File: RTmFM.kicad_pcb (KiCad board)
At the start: 2 copper layers, 122 x 157 mm, 58 parts, among them J1 Conn_02x04_Odd_Even, J2 Conn_01x04, J3 Conn_02x17_Odd_Even, J4 Conn_02x10_Odd_Even, J5 Micro_SD_Card, J6 Conn_01x02, J7 Conn_01x02, U1 SN75176AP, U10 74LS06, U2 SN75176AP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

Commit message: Almost finished HW design
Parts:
- U10, U9: footprint Package_DIP:DIP-14_W10.16mm -> Package_DIP:DIP-14_W7.62mm
- moved J4 143.4 mm to (173.4, 40.2), turned to -90 degrees
- moved J2 130.1 mm to (32.7, 35.5), turned to 0 degrees
- moved U2 126.7 mm to (172.8, 57.2), turned to -90 degrees
- moved C7 125.8 mm to (176.6, 63.4), turned to 90 degrees
- moved R29 121.9 mm to (85.4, 71.1), turned to 180 degrees
- moved R2 117.6 mm to (30.0, 71.2), turned to 0 degrees
- moved C8 113.0 mm to (102.0, 76.2), turned to 180 degrees
- moved R28 111.5 mm to (85.4, 79.1), turned to 180 degrees
- moved J3 111.4 mm to (134.4, 40.2), turned to -90 degrees
- moved C2 111.1 mm to (176.6, 88.8), turned to 90 degrees
- moved U1 110.5 mm to (157.5, 57.2), turned to -90 degrees
- moved U7 109.0 mm to (172.8, 82.5), turned to -90 degrees
- moved C6 108.5 mm to (161.3, 63.5), turned to 90 degrees
- moved R3 106.8 mm to (30.0, 79.2), turned to 0 degrees
- moved R10 104.7 mm to (165.1, 74.9), turned to 0 degrees
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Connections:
- U10 pad 3: /TRACK0 -> /WRITE_FAULT
- U10 pad 4: /ocTRACK0 -> /ocWRITE_FAULT
- U10 pad 5: /WRITE_FAULT -> /INDEX
- U10 pad 6: /ocWRITE_FAULT -> /ocINDEX
- U10 pad 8: /ocINDEX -> /ocTRACK0
- U10 pad 9: /INDEX -> /TRACK0
- U8 pad 39: unconnected-(U8-VSYS-Pad39) -> VCC
- U9 pad 1: /HEAD0 -> /HEAD1
- U9 pad 2: /HSEL0 -> /HSEL1
- U9 pad 3: /HEAD1 -> /HEAD0
- U9 pad 4: /HSEL1 -> /HSEL0
- U9 pad 5: /HEAD2 -> (no net)
- U9 pad 6: /HSEL2 -> (no net)
- U9 pad 8: /RDENA -> /HSEL2
- U9 pad 9: /WRGATE -> /HEAD2
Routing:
- net VCC: track 271.4 -> 620.0 mm, vias 0 -> 4
- net GND: track 0.00 -> 144.0 mm, vias 0 -> 1
- net /DSEL: track 0.00 -> 143.9 mm, vias 0 -> 2
- net /DOUT: track 0.00 -> 110.5 mm, vias 0 -> 1
- net /WDATA: track 0.00 -> 95.3 mm, vias 0 -> 1
- net +12V: track 133.8 -> 217.6 mm
- net /STEP: track 30.4 -> 105.1 mm, vias 0 -> 3
- net /HSEL0: track 0.00 -> 66.9 mm, vias 0 -> 1
- net Net-(J6-Pin_2): track 0.00 -> 63.5 mm, vias 0 -> 1
- net /HSEL2: track 0.00 -> 61.6 mm, vias 0 -> 1
- net /SD_DAT1: track 0.00 -> 60.2 mm
- net /TRACK0: track 16.8 -> 76.8 mm
- net /DIRECTION: track 34.5 -> 93.9 mm, vias 1 -> 3
- net /HSEL1: track 0.00 -> 59.2 mm, vias 0 -> 1
- net /DRV_LED: track 0.00 -> 57.5 mm, vias 0 -> 1
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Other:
- board size 122 x 157 mm -> 157 x 122 mm
- board text added: "+"
- board text added: "0"
- board text added: "1"
- board text added: "12V DUMMY LOAD"
- board text added: "2"
- board text added: "3"
- board text added: "5V DUMMY LOAD"
- board text added: "ACT LED"
- board text added: "DRIVE SELECT"
- board text added: "Designed By Majenko"
- board text added: "M"
- board text added: "RTmFM MFM Emulator Version 1.0"
- board text added: "T"
- board text added: "TERM EN"
- board text added: "majenko.co.uk"

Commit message: End of version 1 design
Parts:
- added H1: MountingHole, MountingHole:MountingHole_3.2mm_M3_DIN965_Pad_TopBottom, F.Cu at (31.0, 45.0)
- added H2: MountingHole, MountingHole:MountingHole_3.2mm_M3_DIN965_Pad_TopBottom, F.Cu at (179.0, 45.0)
- added H3: MountingHole, MountingHole:MountingHole_3.2mm_M3_DIN965_Pad_TopBottom, F.Cu at (31.0, 148.0)
- added H4: MountingHole, MountingHole:MountingHole_3.2mm_M3_DIN965_Pad_TopBottom, F.Cu at (179.0, 148.0)
- added J8: Conn_01x10, Connector_PinHeader_2.54mm:PinHeader_1x10_P2.54mm_Vertical, F.Cu at (165.1, 96.5)
- added R30: 100R, Resistor_THT:R_Axial_DIN0204_L3.6mm_D1.6mm_P7.62mm_Horizontal, F.Cu at (150.0, 106.7)
- added R31: 100R, Resistor_THT:R_Axial_DIN0204_L3.6mm_D1.6mm_P7.62mm_Horizontal, F.Cu at (150.0, 109.2)
- added R32: 100R, Resistor_THT:R_Axial_DIN0204_L3.6mm_D1.6mm_P7.62mm_Horizontal, F.Cu at (150.0, 111.8)
- added R33: 100R, Resistor_THT:R_Axial_DIN0204_L3.6mm_D1.6mm_P7.62mm_Horizontal, F.Cu at (150.0, 114.3)
- added R34: 100R, Resistor_THT:R_Axial_DIN0204_L3.6mm_D1.6mm_P7.62mm_Horizontal, F.Cu at (150.0, 116.8)
- moved R18 6.16 mm to (30.0, 129.0)
- moved R19 6.16 mm to (30.0, 137.0)
- moved R20 6.16 mm to (85.4, 137.0)
- moved R21 6.16 mm to (85.4, 129.0)
- moved R14 6.16 mm to (30.0, 97.0)
- moved R15 6.16 mm to (30.0, 105.0)
- moved R16 6.16 mm to (30.0, 113.0)
- moved R17 6.16 mm to (30.0, 121.0)
- moved R2 6.16 mm to (30.0, 65.0)
- moved R22 6.16 mm to (85.4, 121.0)
- moved R23 6.16 mm to (85.4, 113.0)
- moved R24 6.16 mm to (85.4, 105.0)
- moved R25 6.16 mm to (85.4, 97.0)
- moved R26 6.16 mm to (85.4, 89.0)
- moved R27 6.16 mm to (85.4, 81.0)
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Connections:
- U8 pad 10: unconnected-(U8-GPIO7-Pad10) -> /pSTEP
- U8 pad 11: /DSEL -> /pDIRECTION
- U8 pad 12: /pSTEP -> /pSEEK_CMPLT
- U8 pad 14: /pDIRECTION -> /pTRACK0
- U8 pad 15: /pSEEK_CMPLT -> /pWRITE_FAULT
- U8 pad 16: /pTRACK0 -> /pINDEX
- U8 pad 17: /pWRITE_FAULT -> /pREADY
- U8 pad 19: /pINDEX -> /IO1
- U8 pad 2: unconnected-(U8-GPIO1-Pad2) -> /WDATA
- U8 pad 20: /pREADY -> /IO0
- U8 pad 29: unconnected-(U8-GPIO22-Pad29) -> /IO2
- U8 pad 31: unconnected-(U8-GPIO26_ADC0-Pad31) -> /IO3
- U8 pad 32: unconnected-(U8-GPIO27_ADC1-Pad32) -> /IO4
- U8 pad 4: /WDATA -> /HSEL0
- U8 pad 5: /HSEL0 -> /HSEL1
- U8 pad 6: /HSEL1 -> /HSEL2
- U8 pad 7: /HSEL2 -> /pWRGATE
- U8 pad 9: /pWRGATE -> /DSEL
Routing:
- net VDD: track 35.1 -> 94.9 mm, vias 1 -> 3
- net VCC: track 620.0 -> 675.0 mm, vias 4 -> 22
- net /IO4: track 0.00 -> 33.3 mm
- net /IO3: track 0.00 -> 33.3 mm
- net /IO2: track 0.00 -> 32.3 mm
- net /DSEL: track 143.9 -> 164.1 mm
- net /IO0: track 0.00 -> 14.3 mm
- net /IO1: track 0.00 -> 13.0 mm
- net Net-(J8-Pin_3): track 0.00 -> 10.7 mm
- net Net-(J8-Pin_6): track 0.00 -> 10.7 mm
- net Net-(J8-Pin_4): track 0.00 -> 10.7 mm
- net Net-(J8-Pin_2): track 0.00 -> 10.7 mm
- net Net-(J8-Pin_5): track 0.00 -> 10.7 mm
- net /pWRGATE: track 65.3 -> 73.0 mm, vias 1 -> 0
- net /pINDEX: track 31.5 -> 38.3 mm
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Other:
- outline, holes or cut-outs redrawn
- board text added: "+3.3V"
- board text added: "+5V"
- board text added: "GND"
- board text added: "GPIO14"
- board text added: "GPIO15"
- board text added: "GPIO22"
- board text added: "GPIO26"
- board text added: "GPIO27"
- board text added: "Thanks To: A Swarm Of Dead Insects baljemmett ChloeRaccoon cobhc2015 daftpunkle ddopaz rfprogrammer HotRocksGirl Jeepin247 Karataus82 MoKHelix RemDogKap rhk77 SleepyDeveloper spiesofmud"

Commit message: Exported
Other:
- board text added: "Thanks To: aswarmofdeadinsects BackpackVacuum baljemmett ChloeRaccoon cobhc2015 daftpunkle ddopaz FollowX ginja04 HotRocksGirl Jeepin247 Karataus82 matt_inx MoKHelix pc_magas RemDogKap rfprogrammer rhk77 SeasonedBee SleepyDeveloper spankti spiesofmud StreamElements theOldMaster TokenScandi tradesplatter Tylerhoot vitalkanev Wesley_Nixon Zadster"
- board text removed: "Thanks To: A Swarm Of Dead Insects baljemmett ChloeRaccoon cobhc2015 daftpunkle ddopaz rfprogrammer HotRocksGirl Jeepin247 Karataus82 MoKHelix RemDogKap rhk77 SleepyDeveloper spiesofmud"

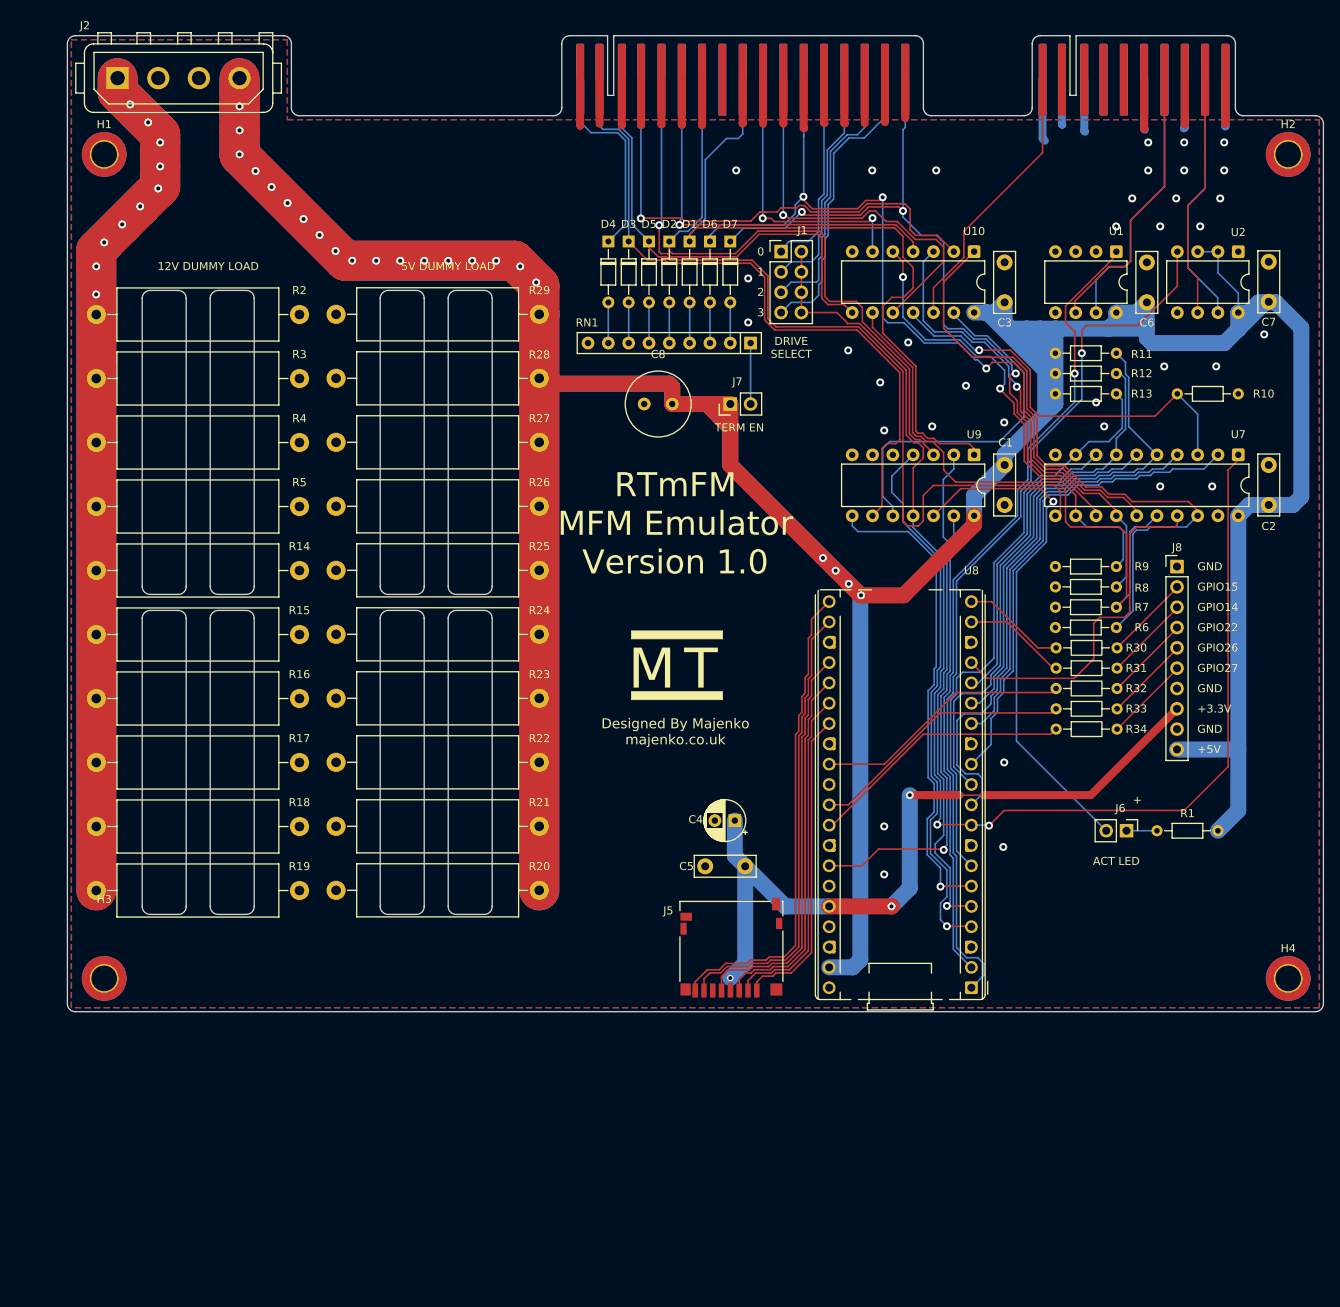
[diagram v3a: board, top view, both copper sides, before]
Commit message: Rework SD interface and add head 4
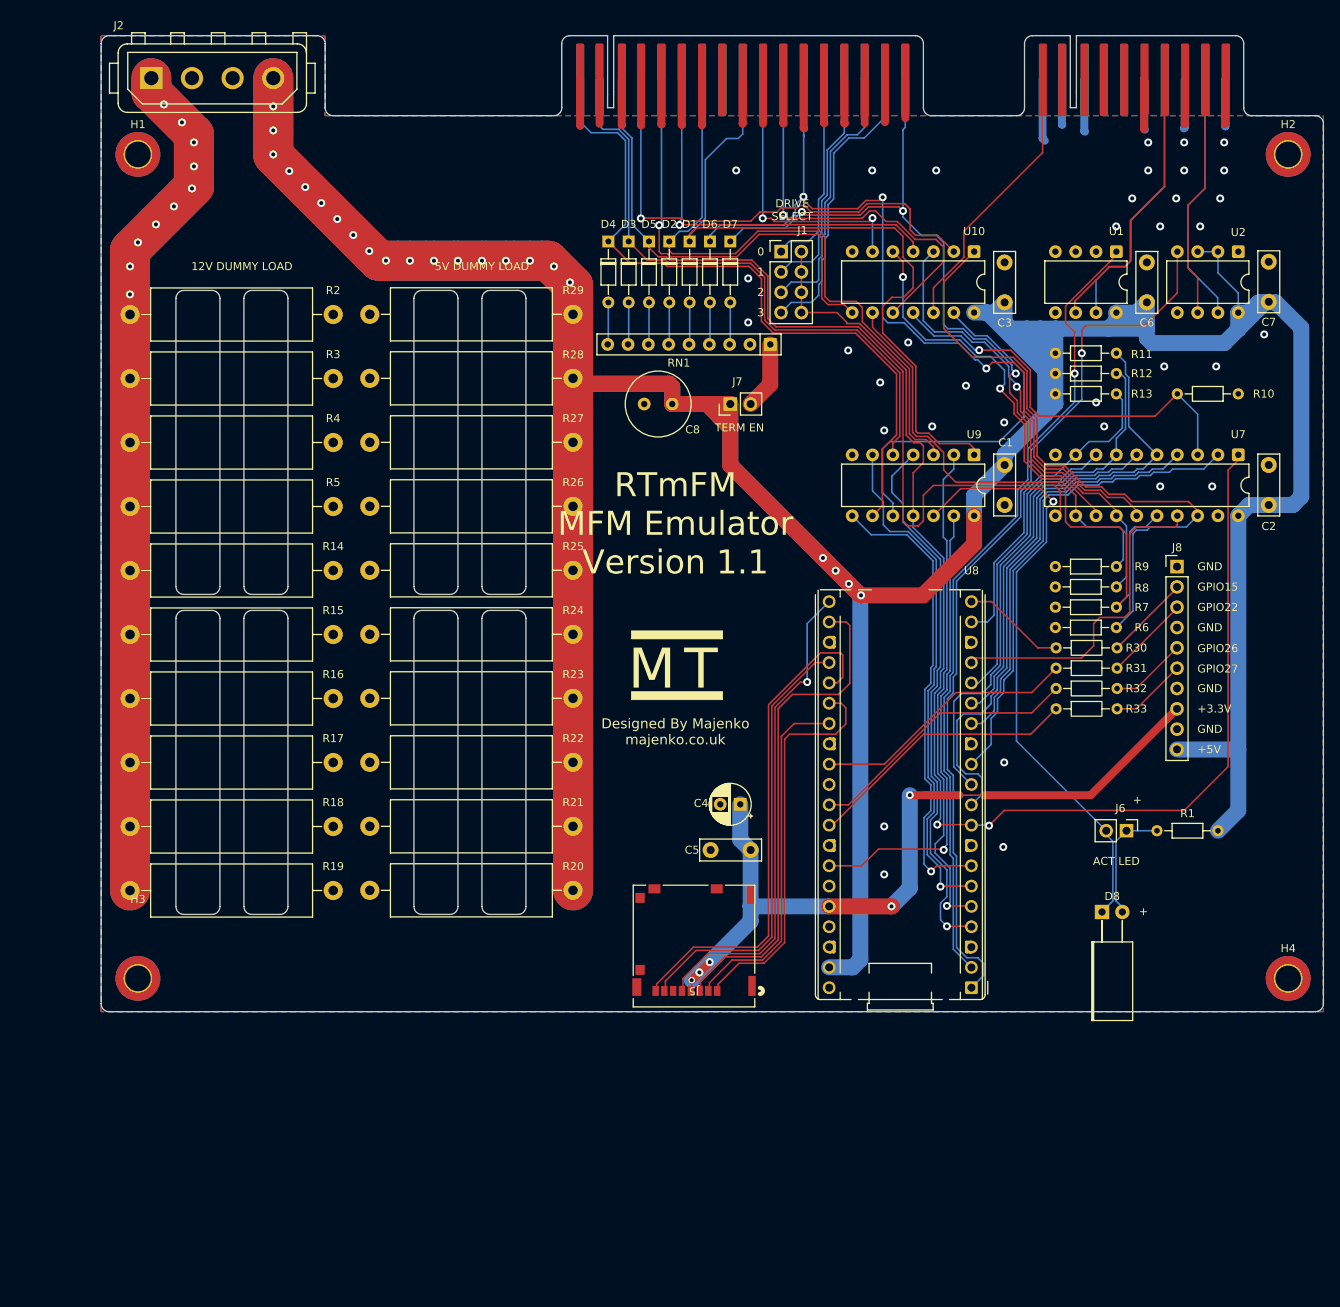
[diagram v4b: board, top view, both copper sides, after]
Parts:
- removed R34: 100R, Resistor_THT:R_Axial_DIN0204_L3.6mm_D1.6mm_P7.62mm_Horizontal
- added D8: LED, LED_THT:LED_Rectangular_W5.0mm_H2.0mm_Horizontal_O3.81mm_Z3.0mm, F.Cu at (155.7, 139.7)
- J5: footprint Connector_Card:microSD_HC_Hirose_DM3D-SF -> footprints:503182-1852_MOL
- moved J5 12.0 mm to (104.7, 155.2), turned to 180 degrees
- moved H1 4.22 mm to (35.2, 45.0)
- moved H3 4.22 mm to (35.2, 148.0)
- moved J2 4.22 mm to (36.9, 35.5)
- moved R14 4.22 mm to (34.2, 97.0)
- moved R15 4.22 mm to (34.2, 105.0)
- moved R16 4.22 mm to (34.2, 113.0)
- moved R17 4.22 mm to (34.2, 121.0)
- moved R18 4.22 mm to (34.2, 129.0)
- moved R19 4.22 mm to (34.2, 137.0)
- moved R2 4.22 mm to (34.2, 65.0)
- moved R3 4.22 mm to (34.2, 73.0)
- moved R4 4.22 mm to (34.2, 81.0)
- moved R5 4.22 mm to (34.2, 89.0)
- moved R20 4.22 mm to (89.6, 137.0)
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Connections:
- J8 pad 4: Net-(J8-Pin_4) -> GND
- R32 pad 2: Net-(J8-Pin_4) -> Net-(J8-Pin_5)
- R33 pad 2: Net-(J8-Pin_5) -> Net-(J8-Pin_6)
- RN1 pad 2: Net-(D7-A) -> unconnected-(RN1-R1-Pad2)
- RN1 pad 3: Net-(D6-A) -> Net-(D7-A)
- RN1 pad 4: Net-(D1-A) -> Net-(D6-A)
- RN1 pad 5: Net-(D2-A) -> Net-(D1-A)
- RN1 pad 6: Net-(D5-A) -> Net-(D2-A)
- RN1 pad 7: Net-(D3-A) -> Net-(D5-A)
- RN1 pad 8: Net-(D4-A) -> Net-(D3-A)
- RN1 pad 9: unconnected-(RN1-R8-Pad9) -> Net-(D4-A)
- U8 pad 19: /IO1 -> /pWRGATE
- U8 pad 21: /SD_DAT1 -> /SD_CLK
- U8 pad 22: /SD_DAT0 -> /SD_CMD
- U8 pad 24: /SD_CLK -> /SD_DAT0
- U8 pad 25: /SD_CMD -> /SD_DAT1
- U8 pad 26: /SD_DAT3 -> /SD_DAT2
- U8 pad 27: /SD_DAT2 -> /SD_DAT3
- U8 pad 29: /IO2 -> /IO1
- U8 pad 31: /IO3 -> /IO2
- U8 pad 32: /IO4 -> /IO3
- U8 pad 7: /pWRGATE -> /HSEL3
- U9 pad 5: (no net) -> /HEAD2
- U9 pad 6: (no net) -> /HSEL2
- U9 pad 8: /HSEL2 -> /HSEL3
- U9 pad 9: /HEAD2 -> /HEAD3
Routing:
- net /HEAD3: track 25.4 -> 90.4 mm
- net /HSEL3: track 0.00 -> 58.0 mm, vias 0 -> 1
- net /IO4: track 33.3 -> 0.00 mm
- net /pWRGATE: track 73.0 -> 40.3 mm
- net /IO1: track 13.0 -> 33.7 mm
- net /SD_CMD: track 45.8 -> 62.4 mm
- net Net-(D8-K): track 64.8 -> 75.8 mm
- net Net-(D8-A): track 3.81 -> 14.8 mm
- net /SD_DAT2: track 39.0 -> 49.7 mm
- net Net-(J8-Pin_4): track 10.7 -> 0.00 mm
- net /SD_CLK: track 50.4 -> 60.7 mm, vias 0 -> 1
- net /HEAD2: track 86.7 -> 77.4 mm
- net VCC: track 675.0 -> 668.0 mm
- net VDD: track 94.9 -> 100.0 mm, vias 3 -> 5
- net /HSEL2: track 60.1 -> 64.3 mm
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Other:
- board size 157 x 122 mm -> 152.8 x 122 mm
- board text added: "RTmFM MFM Emulator Version 1.1"
- board text removed: "GPIO14"
- board text removed: "RTmFM MFM Emulator Version 1.0"

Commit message: Version 1.1 rework
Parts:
- added J9: Conn_02x15_Odd_Even, Connector_PinHeader_2.54mm:PinHeader_2x15_P2.54mm_Vertical, F.Cu at (155.2, 97.2)
- moved R6 10.4 mm to (156.9, 114.5)
- moved R7 10.4 mm to (156.9, 112.0)
- moved R8 10.4 mm to (156.9, 109.4)
- moved R9 10.4 mm to (156.9, 106.9)
- moved R30 10.4 mm to (149.4, 117.0)
- moved R31 10.4 mm to (149.4, 119.6)
- moved R32 10.4 mm to (149.4, 122.1)
- moved R33 10.4 mm to (149.4, 124.7)
- moved H4 8.06 mm to (175.0, 155.0)
- moved D8 7.97 mm to (155.1, 147.6)
- moved U8 7.40 mm to (138.4, 156.5)
- moved C5 7.40 mm to (110.8, 139.3)
- moved J5 7.40 mm to (103.7, 162.5)
- moved C4 7.40 mm to (109.5, 133.6)
- moved H3 7.00 mm to (35.0, 155.0)
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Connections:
- U8 pad 1: /DOUT -> /xDOUT
- U8 pad 10: /pSTEP -> /xpSTEP
- U8 pad 11: /pDIRECTION -> /xpDIRECTION
- U8 pad 12: /pSEEK_CMPLT -> /xpSEEK_CMPLT
- U8 pad 14: /pTRACK0 -> /xpTRACK0
- U8 pad 15: /pWRITE_FAULT -> /xpWRITE_FAULT
- U8 pad 16: /pINDEX -> /xpINDEX
- U8 pad 17: /pREADY -> /xpREADY
- U8 pad 19: /pWRGATE -> /xpWRGATE
- U8 pad 2: /WDATA -> /xWDATA
- U8 pad 4: /HSEL0 -> /xHSEL0
- U8 pad 5: /HSEL1 -> /xHSEL1
- U8 pad 6: /HSEL2 -> /xHSEL2
- U8 pad 7: /HSEL3 -> /xHSEL3
- U8 pad 9: /DSEL -> /xDSEL
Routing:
- net /xHSEL0: track 0.00 -> 63.1 mm, vias 0 -> 1
- net /xHSEL3: track 0.00 -> 61.3 mm, vias 0 -> 1
- net /xDOUT: track 0.00 -> 61.2 mm
- net /xHSEL2: track 0.00 -> 60.2 mm, vias 0 -> 1
- net /xWDATA: track 0.00 -> 58.0 mm
- net /xHSEL1: track 0.00 -> 55.4 mm, vias 0 -> 1
- net /DSEL: track 164.2 -> 111.2 mm, vias 2 -> 0
- net /DOUT: track 111.6 -> 59.5 mm
- net /HSEL0: track 68.3 -> 18.8 mm, vias 1 -> 0
- net /HSEL3: track 58.0 -> 8.94 mm, vias 1 -> 0
- net /xDSEL: track 0.00 -> 47.5 mm, vias 0 -> 1
- net /HSEL2: track 64.3 -> 17.7 mm, vias 1 -> 0
- net /WDATA: track 100.7 -> 55.2 mm
- net /xpSTEP: track 0.00 -> 44.4 mm
- net /HSEL1: track 62.4 -> 18.1 mm, vias 1 -> 0
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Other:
- board size 152.8 x 122 mm -> 150 x 130 mm
- board text added: "DIR"
- board text added: "DOUT"
- board text added: "DSEL"
- board text added: "HSEL0"
- board text added: "HSEL1"
- board text added: "HSEL2"
- board text added: "HSEL3"
- board text added: "INDEX"
- board text added: "READY"
- board text added: "SEEKOK"
- board text added: "STEP"
- board text added: "TRK0"
- board text added: "Thanks To: aswarmofdeadinsects BackpackVacuum baljemmett cdxxxxdxdrtx ChloeRaccoon cobhc2015 daftpunkle ddopaz FollowX ginja04 HotRocksGirl Jeepin247 Karataus82 matt_inx MB60893 MoKHelix pc_magas rasz_pl RemDogKap rfprogrammer rhk77 SeasonedBee SleepyDeveloper spankti spiesofmud StreamElements theOldMaster TokenScandi tradesplatter Tylerhoot vitalkanev Wesley_Nixon Zadster"
- board text added: "WDATA"
- board text added: "WRFLT"
- board text added: "WRGATE"
- board text removed: "Thanks To: aswarmofdeadinsects BackpackVacuum baljemmett ChloeRaccoon cobhc2015 daftpunkle ddopaz FollowX ginja04 HotRocksGirl Jeepin247 Karataus82 matt_inx MoKHelix pc_magas RemDogKap rfprogrammer rhk77 SeasonedBee SleepyDeveloper spankti spiesofmud StreamElements theOldMaster TokenScandi tradesplatter Tylerhoot vitalkanev Wesley_Nixon Zadster"

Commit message: Revision 1.1 and working data out
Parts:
- removed D1, D2, D3, D4, D5, D6, D7: BAT43, Diode_THT:D_DO-34_SOD68_P7.62mm_Horizontal
- removed J7: Conn_01x02, Connector_PinHeader_2.54mm:PinHeader_1x02_P2.54mm_Vertical
- removed RN1: 330R, Resistor_THT:R_Array_SIP9
- added R34: 220/330, Package_DIP:DIP-14_W7.62mm_Socket, F.Cu at (108.6, 57.0)
- moved J6 13.5 mm to (157.5, 142.8)
- moved R1 13.5 mm to (169.4, 142.8)
- moved D8 0.38 mm to (155.0, 148.0)
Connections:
- U8 pad 20: /IO0 -> /DRV_LED
- U8 pad 29: /IO1 -> /IO0
- U8 pad 31: /IO2 -> /IO1
- U8 pad 32: /IO3 -> /IO2
- U8 pad 34: /DRV_LED -> /IO3
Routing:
- net /DRV_LED: track 71.8 -> 27.4 mm
- net VCC: track 680.2 -> 703.8 mm
- net VDD: track 112.2 -> 132.4 mm, vias 5 -> 3
- net /IO0: track 17.0 -> 33.6 mm
- net Net-(D8-A): track 23.0 -> 9.37 mm
- net Net-(J7-Pin_2): track 8.47 -> 0.00 mm
- net /HEAD0: track 80.4 -> 86.5 mm
- net Net-(D7-A): track 5.08 -> 0.00 mm
- net Net-(D6-A): track 5.08 -> 0.00 mm
- net Net-(D5-A): track 5.08 -> 0.00 mm
- net Net-(D4-A): track 5.08 -> 0.00 mm
- net Net-(D3-A): track 5.08 -> 0.00 mm
- net Net-(D2-A): track 5.08 -> 0.00 mm
- net Net-(D1-A): track 5.08 -> 0.00 mm
- net /ocTRACK0: track 56.6 -> 61.3 mm
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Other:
- outline, holes or cut-outs redrawn
- board text added: "TERMINATION 220/330"
